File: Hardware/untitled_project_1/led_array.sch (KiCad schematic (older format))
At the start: 157 parts

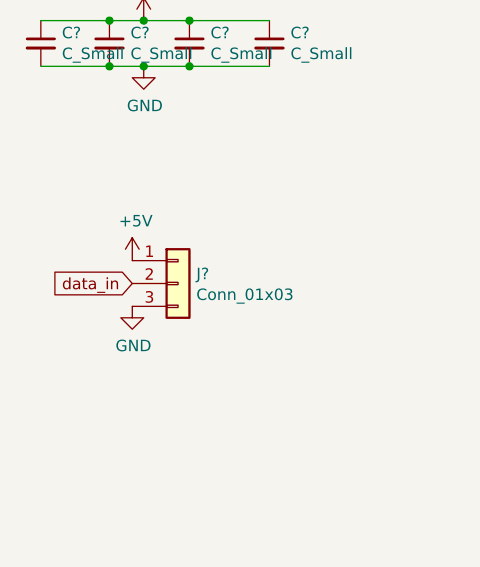
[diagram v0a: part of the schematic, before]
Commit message: add power and programming schematics
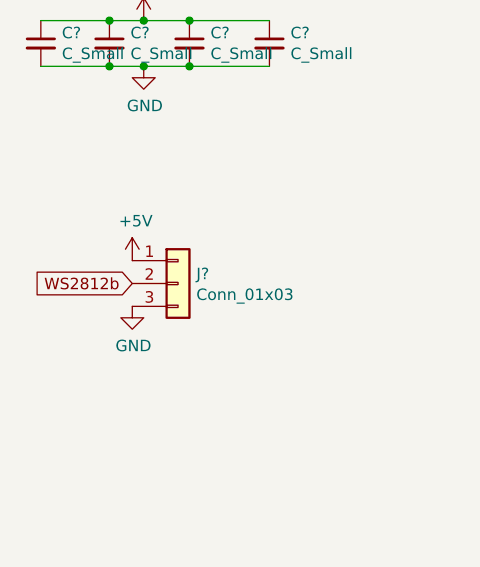
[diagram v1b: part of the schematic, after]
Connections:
- net data_in: no longer J?.2 (Pin_2)
- new net WS2812b: J?.2 (Pin_2)
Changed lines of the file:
@@
 $Descr A3 16535 11693
 encoding utf-8
-Sheet 3 3
+Sheet 2 3
 Title ""
 Date ""
@@
 data_in
 Text GLabel 1600 3700 0    50   Input ~ 0
-data_in
+WS2812b
 Wire Wire Line
 	3150 1500 3600 1500

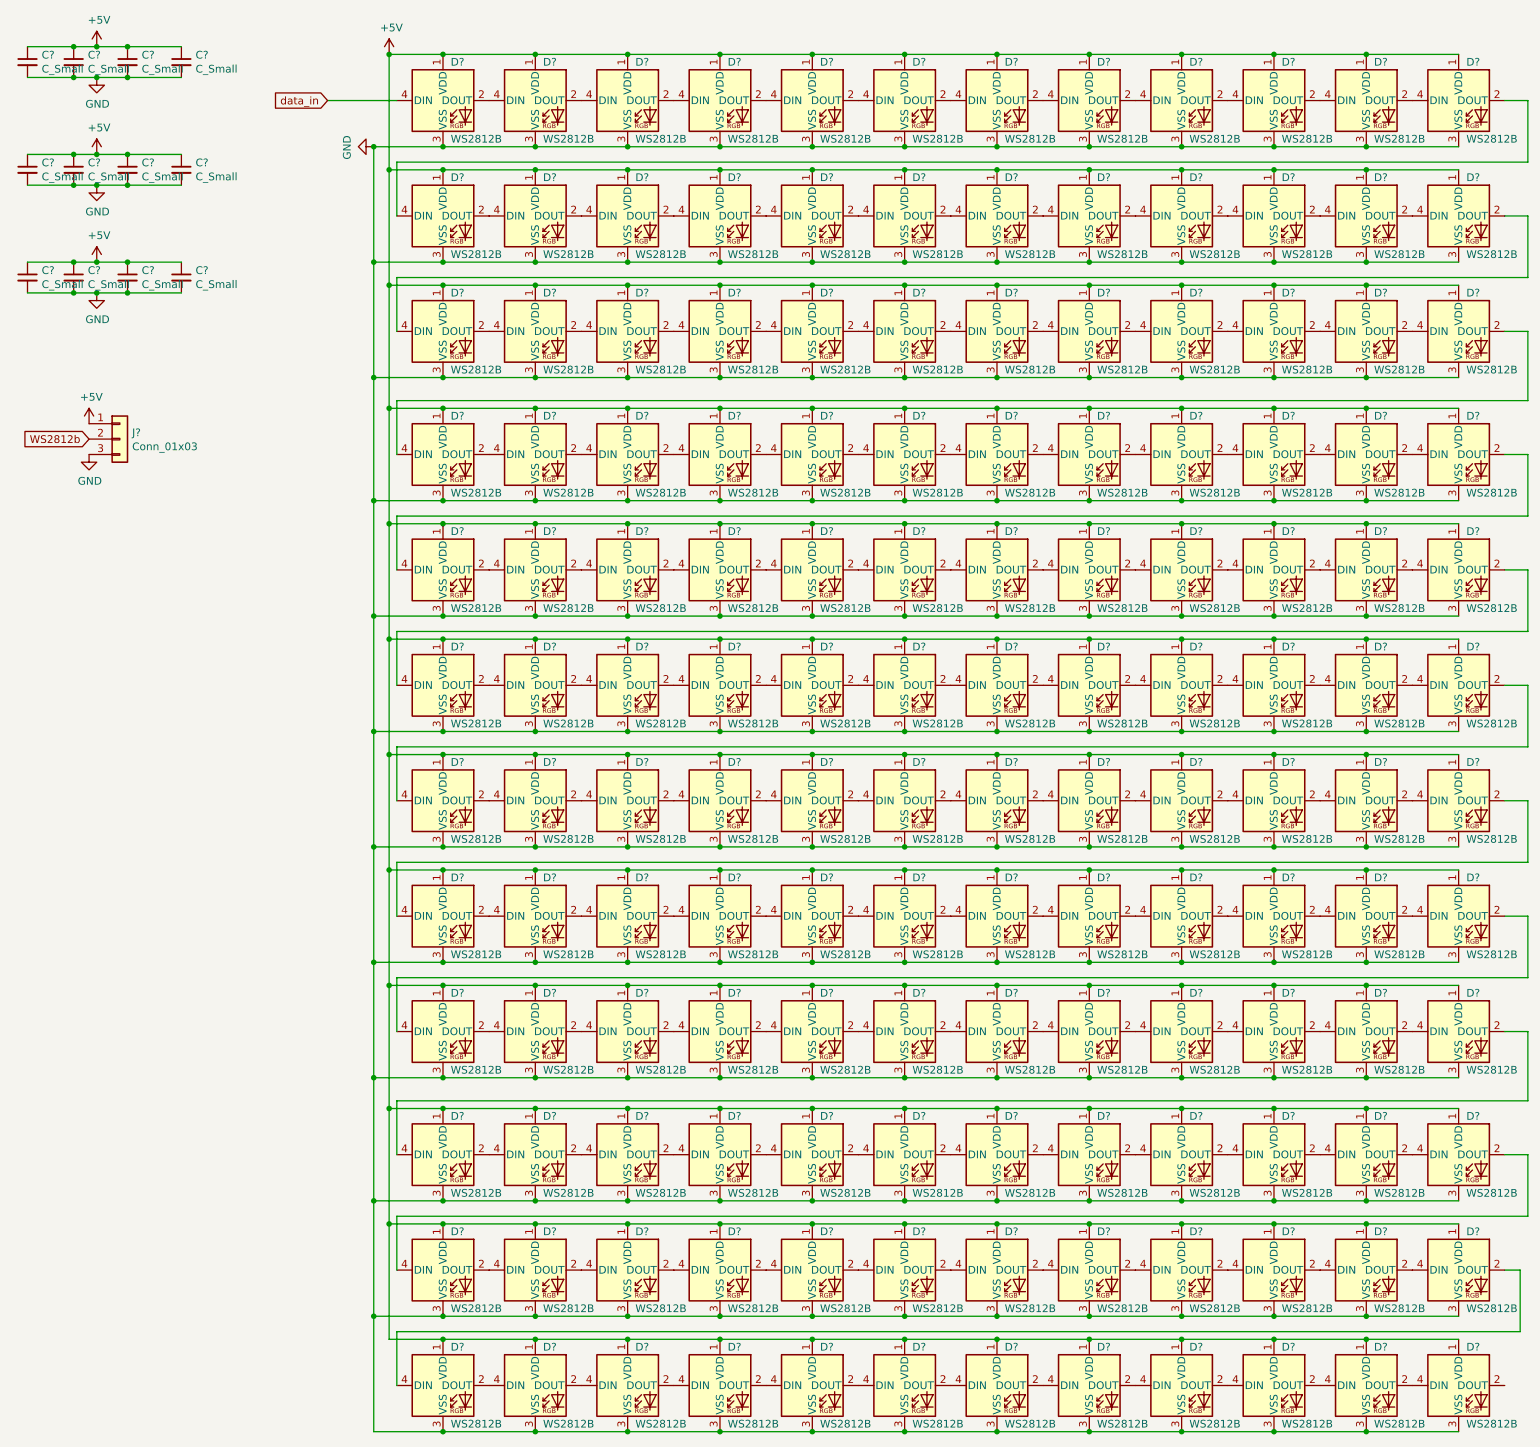
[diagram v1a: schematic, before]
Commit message: add footprints to szymbols:
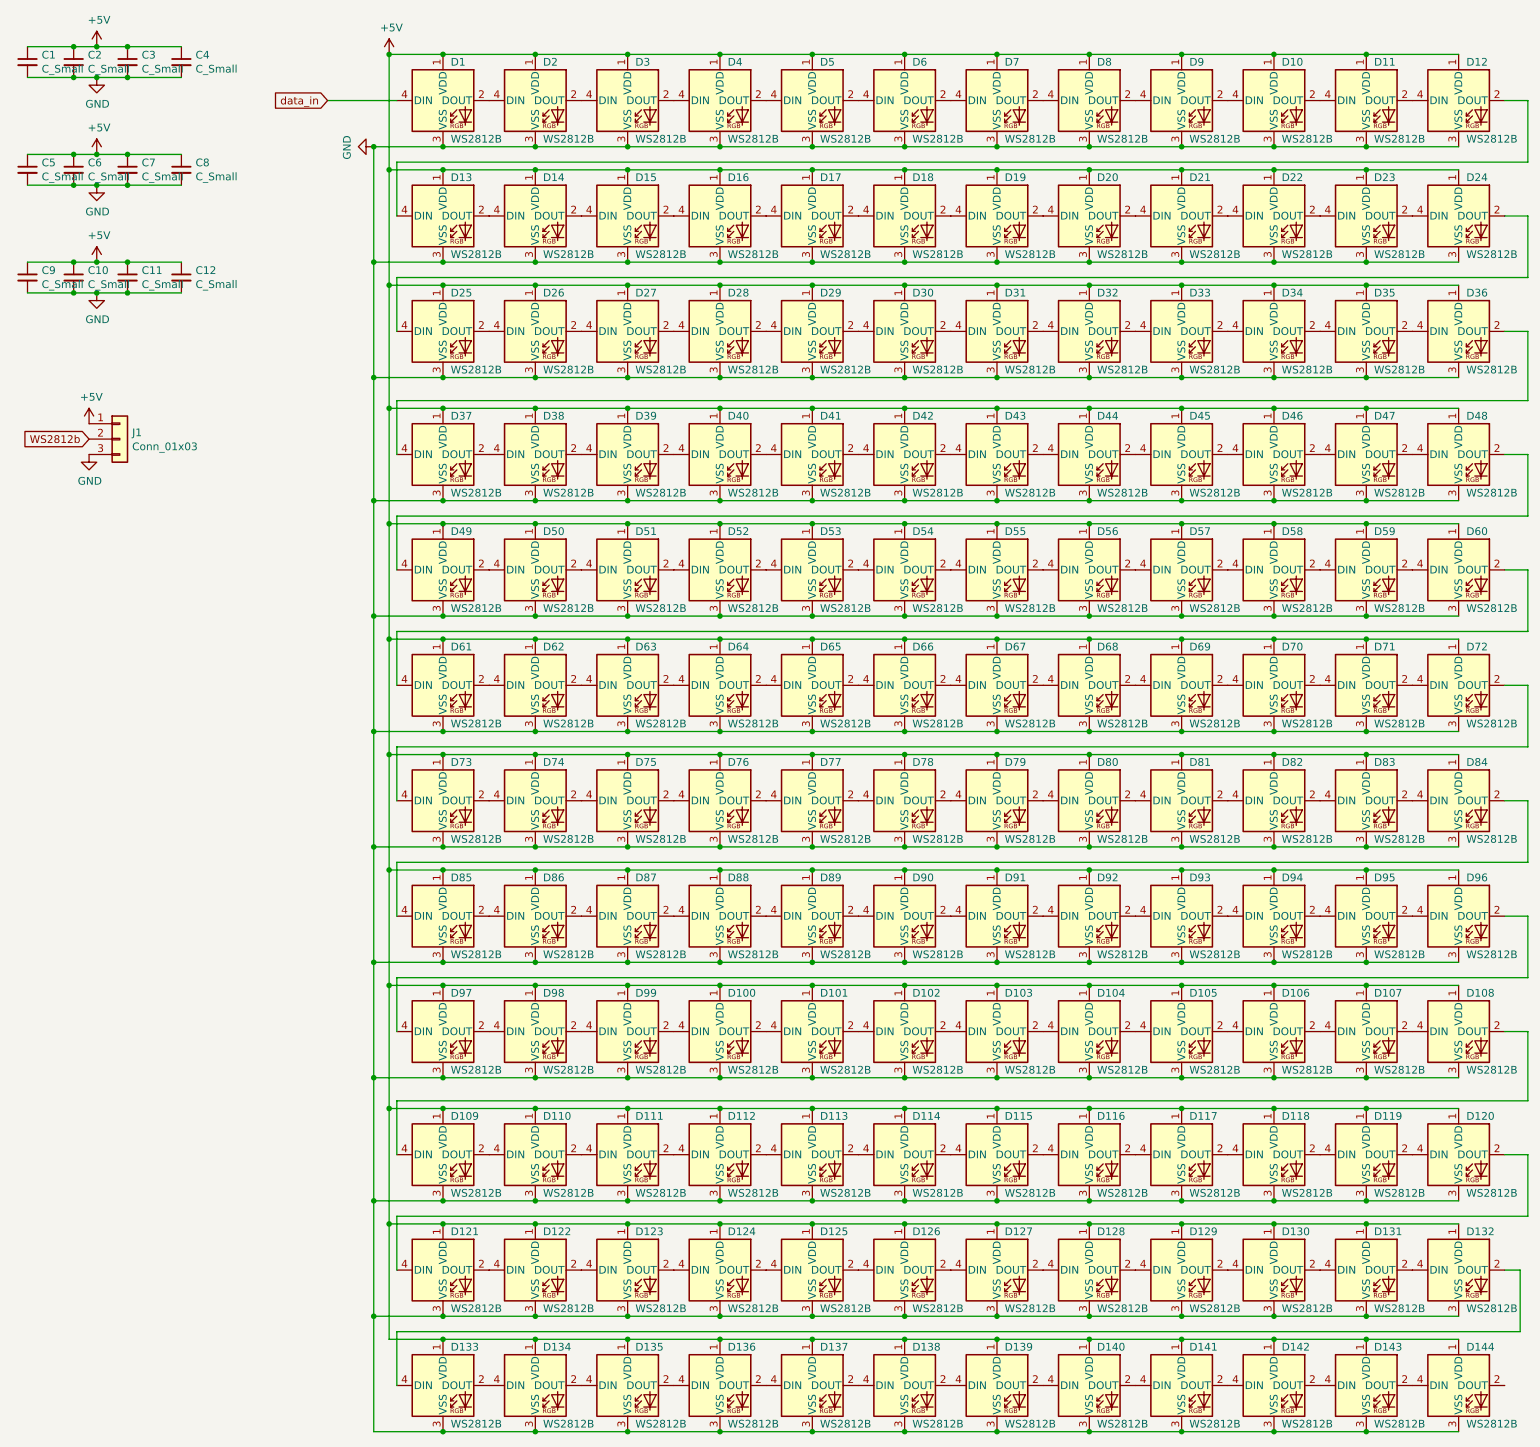
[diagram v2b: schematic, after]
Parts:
- C1, C10, C11, C12, C2, C3, C4, C5, C6, C7, C8, C9: renamed from C?; footprint (none) -> Capacitor_SMD:C_1210_3225Metric_Pad1.42x2.65mm_HandSolder
- gave numbers to parts that had none: 145
